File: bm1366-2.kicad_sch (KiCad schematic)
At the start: 59 parts, among them U13 ADP171AUJ-R7, U14 BM1366_mode1, U23 ADP171AUJ-R7

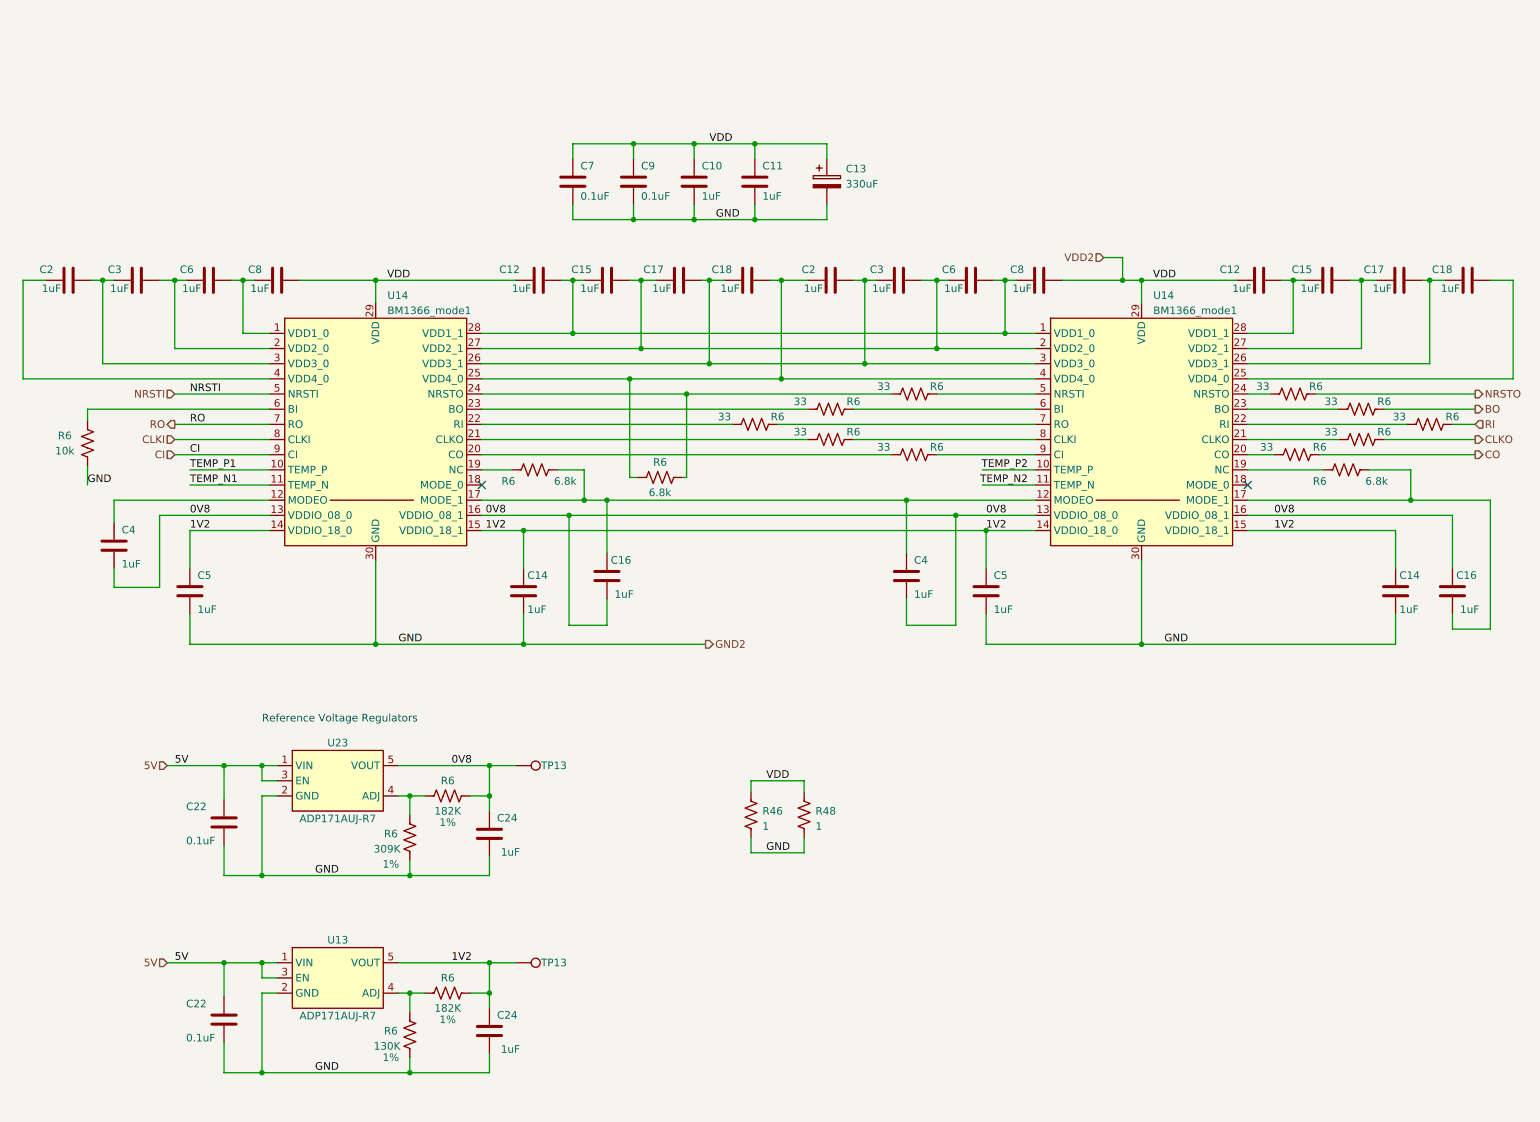
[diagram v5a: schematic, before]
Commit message: added enclosure edge cuts. added heatsink outline. changed the two middle voltage domain ASICs to mode 0 so the data lines can snake through all 6 chips.
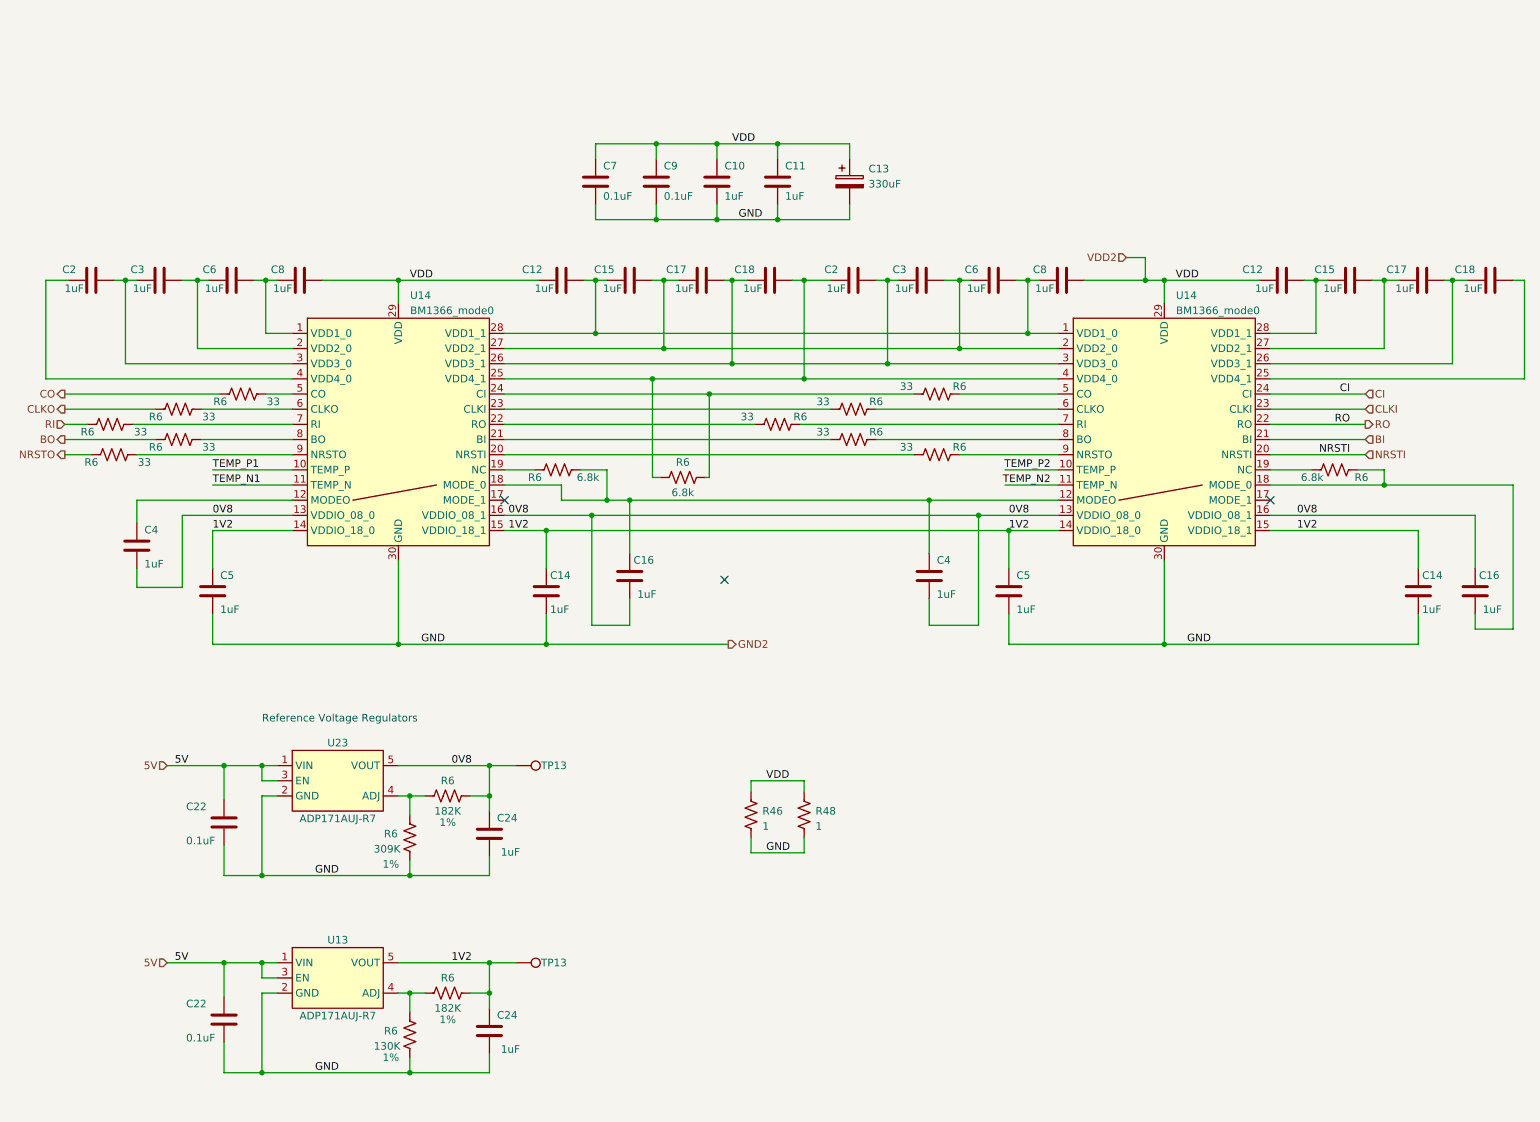
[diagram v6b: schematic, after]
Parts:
- removed R6: 10k, Resistor_SMD:R_0402_1005Metric, symbol Device:R_US
- U14: value BM1366_mode1 -> BM1366_mode0; symbol bitaxe:BM1366_mode1 -> bitaxe:BM1366_mode0
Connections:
- net CI: now also U14.24 (CI); no longer U14.9 (CI)
- net CLKI: now also U14.23 (CLKI); no longer U14.8 (CLKI)
- net NRSTI: now also U14.20 (NRSTI); no longer U14.5 (NRSTI)
- net RO: now also U14.22 (RO); no longer U14.7 (RO)
- net at R6.1: now also U14.9 (NRSTO); no longer U14.24 (NRSTO)
- net at R6.1: now also U14.7 (RI); no longer U14.22 (RI)
- net at R6.1: now also U14.8 (BO); no longer U14.23 (BO)
- net at U14.6 (CLKO): now also R6.1
- net at R6.1: now also U14.5 (CO); no longer U14.20 (CO)
- net BI: now reaches U14.21 (BI)
- net BI: no longer R6.1
- net at C16.1, C4.1, R6.2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: now also U14.18 (MODE_0); no longer U14.17 (MODE_1)
- net at R6.1: now also C16.2, U14.18 (MODE_0); no longer U14.19 (NC)
- new net: R6.2, U14.19 (NC)
- now unconnected: U14.17 (MODE_1)
- no-connect marks 2 -> 3
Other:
- moved on the sheet: C10, C11, C12, C13, C14, C15, C16, C17, C18, C2, C3, C4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

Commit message: add level translator circuits to ASIC communications
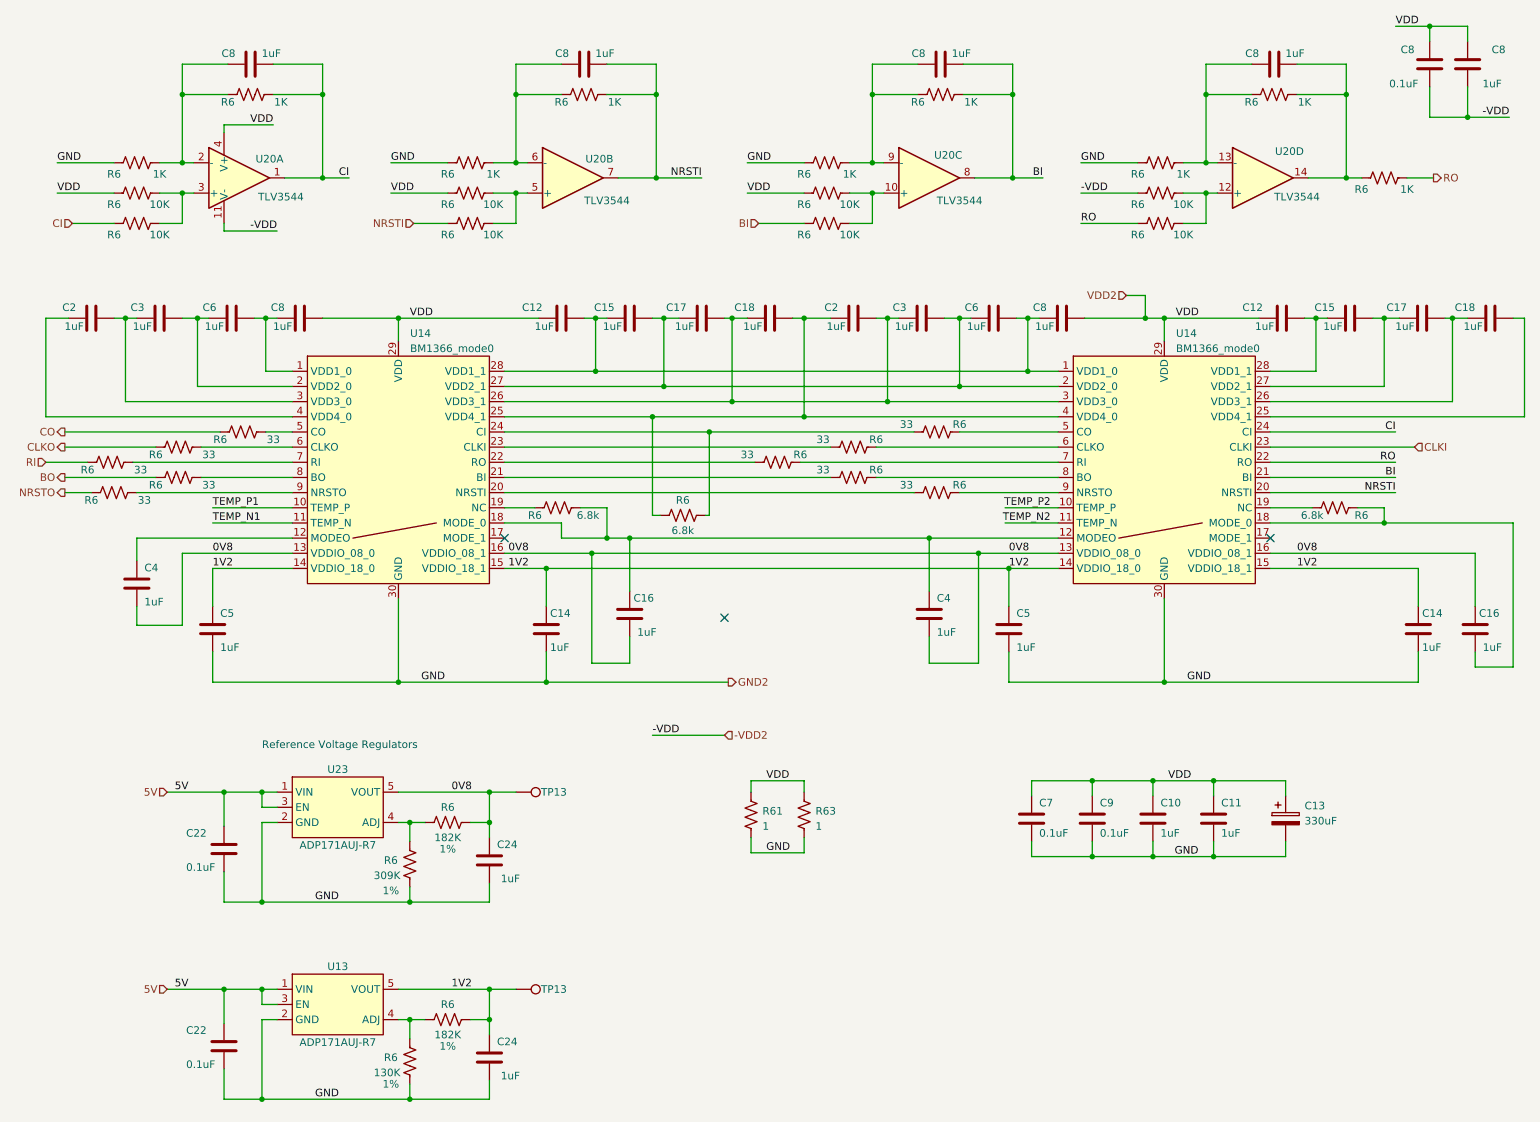
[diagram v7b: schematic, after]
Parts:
- added C8 (x5): 1uF, Capacitor_SMD:C_0402_1005Metric, symbol Device:C
- added C8: 0.1uF, Capacitor_SMD:C_0402_1005Metric, symbol Device:C
- added R6 (x8): 10K, Resistor_SMD:R_0402_1005Metric, symbol Device:R_US
- added R6 (x9): 1K, Resistor_SMD:R_0402_1005Metric, symbol Device:R_US
- added U20: TLV3544, Package_SO:TSSOP-14_4.4x5mm_P0.65mm, symbol bitaxe:TLV3544
- renumbered R46 to R61, R48 to R63
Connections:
- net BI: now also C8.2, R6.1, R6.1, U20.8
- net CI: now also C8.2, R6.1, R6.1, U20.1
- net GND2: now also R6.2, R6.2, R6.2, R6.2
- net NRSTI: now also C8.2, R6.1, R6.1, U20.7
- net RO: now also R6.1, R6.1
- net VDD2: now also C8.2, C8.2, R6.1, R6.1, R6.1, U20.4 (V+)
- new net: R6.2, R6.2, U20.12 (+)
- new net: C8.1, R6.1, R6.2, U20.2 (-)
- new net: C8.1, R6.1, R6.2, U20.9 (-)
- new net: R6.2, R6.2, U20.5 (+)
- new net: C8.1, R6.1, R6.2, U20.13 (-)
- new net: C8.2, R6.1, R6.2, U20.14
- new net: C8.1, R6.1, R6.2, U20.6 (-)
- new net: R6.2, R6.2, U20.10 (+)
- new net: R6.2, R6.2, U20.3 (+)
- new net -VDD2: C8.1, C8.1, R6.1, U20.11 (V-)
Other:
- moved on the sheet: C10, C11, C12, C13, C14, C15, C16, C17, C18, C2, C22, C24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

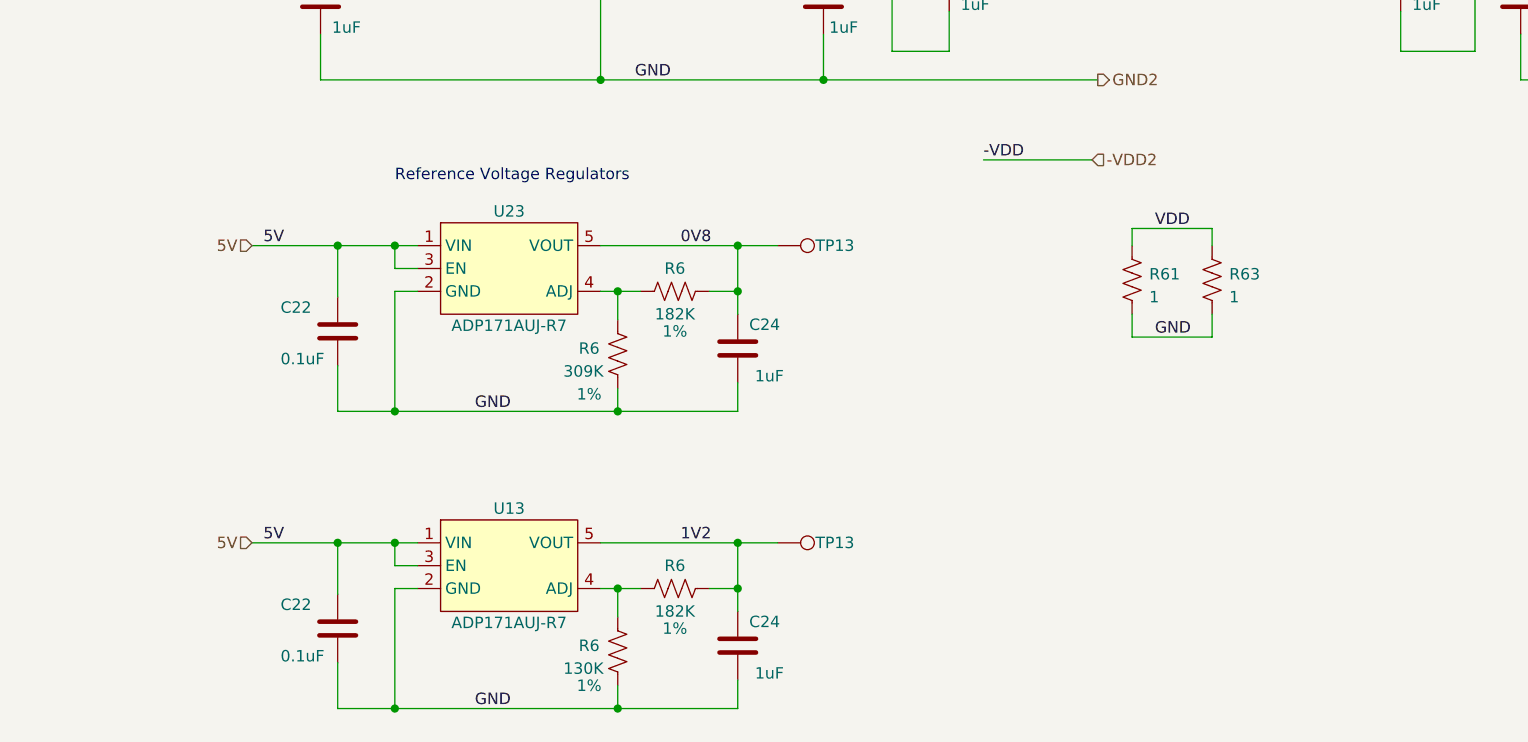
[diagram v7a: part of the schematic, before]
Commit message: Update temperature sensors, start deep review
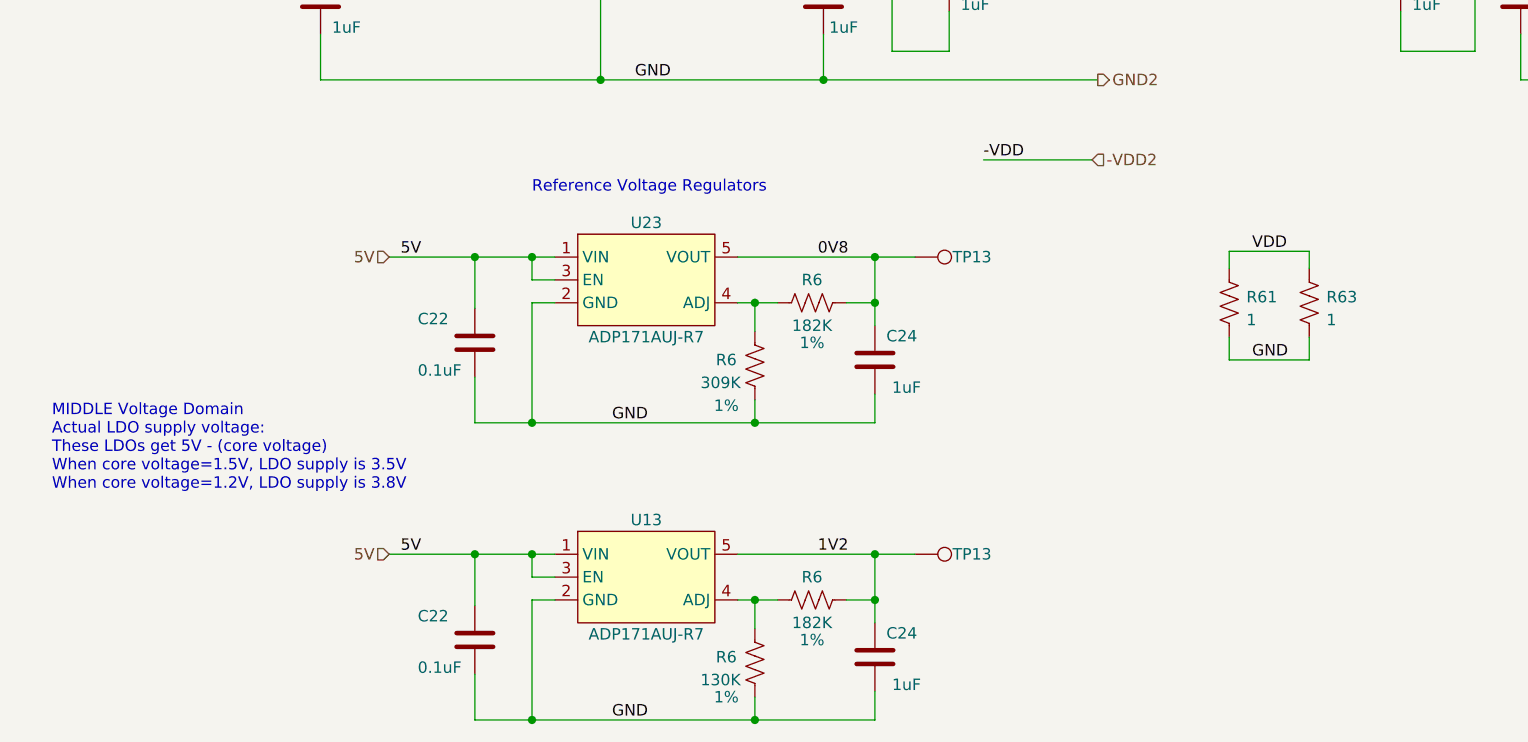
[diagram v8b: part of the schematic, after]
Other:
- note added: "MIDDLE Voltage Domain Actual LDO supply voltage: These LDOs get 5V - (core voltage) When core voltage=1.5V, LDO supply is 3.5V When core voltage=1.2V, LDO supply is 3.8V"
- moved on the sheet: C22, C24, R6, R61, R63, TP13, U13, U23
